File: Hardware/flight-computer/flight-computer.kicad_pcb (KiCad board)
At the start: 4 copper layers, 25.4 x 51.5 mm, 42 parts, among them J1 Conn_01x06_Pin, J2 Conn_01x06_Pin, J3 Power Connector, J4 Micro_SD_Card, J5 USB_C_Receptacle_USB2.0_16P, J6 Conn_01x02_Pin, Q1 DMN3404L, Q2 DMN3404L, U1 LMR51420X, U2 ESP32-S3-WROOM-1, U3 LSM6DSO32TR, U4 INA2180A1IDGKR

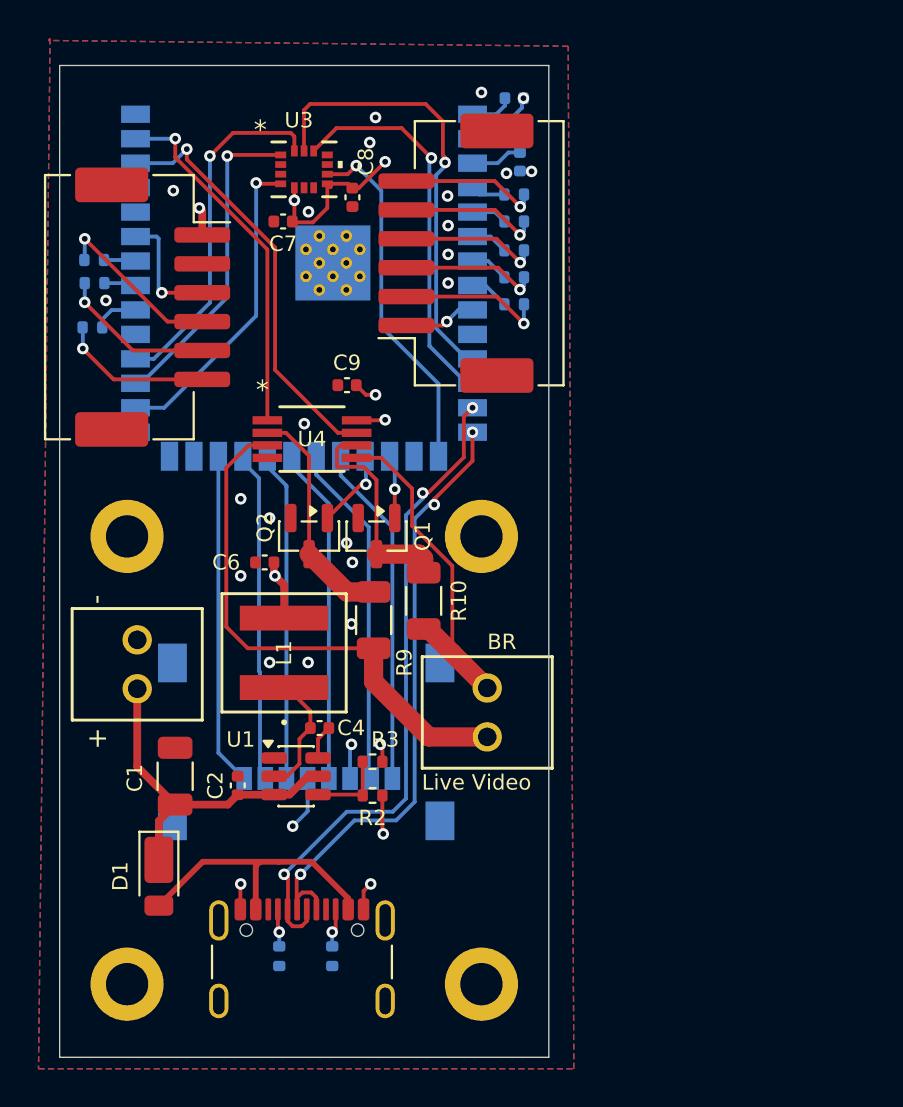
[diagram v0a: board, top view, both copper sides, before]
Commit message: added barometer and 10p conn to esp
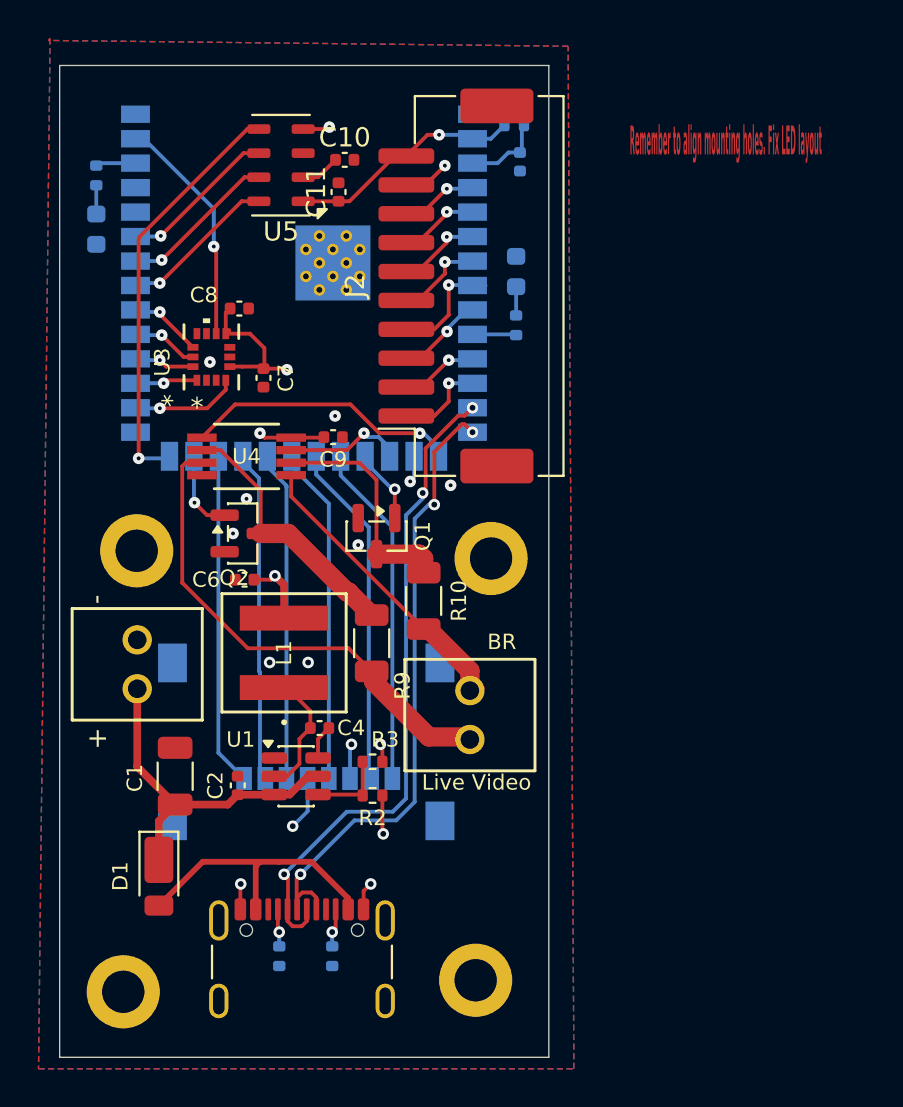
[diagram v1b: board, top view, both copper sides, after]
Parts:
- removed J1: Conn_01x06_Pin, Connector_JST:JST_ZE_SM06B-ZESS-TB_1x06-1MP_P1.50mm_Horizontal
- removed R11, R12, R13, R14, R15, R8: 200 Ohm, Resistor_SMD:R_0402_1005Metric
- added C10: 100nF, Capacitor_SMD:C_0402_1005Metric, F.Cu at (146.9, 83.6)
- added C11: 10uF, Capacitor_SMD:C_0402_1005Metric, F.Cu at (146.6, 85.3)
- added D2: LED, LED_SMD:LED_0603_1608Metric, B.Cu at (134.0, 87.2)
- added D3: LED, LED_SMD:LED_0603_1608Metric, B.Cu at (155.8, 89.4)
- added U5: MPL3115A2, Package_LGA:NXP_LGA-8_3x5mm_P1.25mm_H1.1mm, F.Cu at (143.6, 83.9)
- J2: value Conn_01x06_Pin -> Conn_01x10_Pin; footprint Connector_JST:JST_ZE_SM06B-ZESS-TB_1x06-1MP_P1.50mm_Horizontal -> Connector_JST:JST_ZE_SM10B-ZESS-TB_1x10-1MP_P1.50mm_Horizontal
- R10, R9: value 100 mOhm -> 15 mOhm
- R6, R7: value 200 Ohm -> 220
- moved H2 23.0 mm to (153.7, 126.2)
- moved H3 22.5 mm to (136.1, 103.9)
- moved R7 22.2 mm to (155.8, 92.2), turned to 90 degrees
- moved H1 18.9 mm to (154.5, 104.3)
- moved H4 18.6 mm to (135.4, 126.8)
- moved U3 10.9 mm to (140.0, 93.9), turned to 90 degrees
- moved C8 8.24 mm to (141.4, 91.4), turned to 0 degrees
- moved C7 8.19 mm to (142.7, 95.0), turned to -90 degrees
- moved R6 7.89 mm to (134.0, 84.5), turned to -90 degrees
- moved U4 3.52 mm to (141.8, 99.0)
- moved Q2 3.45 mm to (141.6, 103.0), turned to 0 degrees
- moved C9 2.79 mm to (146.3, 98.0), turned to 180 degrees
- moved J2 1.70 mm to (152.7, 90.2)
- moved C6 1.38 mm to (141.7, 105.4)
- moved R9 1.20 mm to (148.3, 108.7)
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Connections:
- J2 pad 1: FIN_RST -> FIN4_RX
- J2 pad 2: Net-(J2-Pin_2) -> FIN4_TX
- J2 pad 3: Net-(J2-Pin_3) -> FIN3_RX
- J2 pad 4: Net-(J2-Pin_4) -> FIN3_TX
- J2 pad 5: Net-(J2-Pin_5) -> FIN2_RX
- J2 pad 6: Net-(J2-Pin_6) -> FIN2_TX
- Q1 pad 1: Remote Start 1 -> Remote Start 2
- Q2 pad 1: Remote Start 2 -> Remote Start 1
- R6 pad 1: Net-(J1-Pin_6) -> Net-(U2-IO2)
- R6 pad 2: FIN_SCK -> Net-(D2-A)
- R7 pad 1: Net-(J1-Pin_4) -> Net-(U2-IO17)
- R7 pad 2: FIN_MOSI -> Net-(D3-A)
- U2 pad 10: unconnected-(U2-IO17-Pad10) -> Net-(U2-IO17)
- U2 pad 11: LSM_SCK -> FIN4_TX
- U2 pad 12: LSM_CS -> FIN4_RX
- U2 pad 15: LSM_INT2 -> IMP_OUT1
- U2 pad 17: Remote Start 1 -> IMP_OUT2
- U2 pad 25: unconnected-(U2-IO48-Pad25) -> Remote Start 1
- U2 pad 26: unconnected-(U2-IO45-Pad26) -> MPL_INT2
- U2 pad 31: unconnected-(U2-IO38-Pad31) -> LSM_SCK
- U2 pad 32: FIN_SCK -> LSM_CS
- U2 pad 33: FIN_MISO -> MPL_SCL
- U2 pad 34: FIN_MOSI -> MPL_SDA
- U2 pad 35: FIN_DRDY -> MPL_INT1
- U2 pad 38: IMP_OUT2 -> Net-(U2-IO2)
- U2 pad 39: IMP_OUT1 -> LSM_INT2
- U2 pad 4: FIN_CS1 -> FIN1_TX
- U2 pad 5: FIN_CS2 -> FIN1_RX
- U2 pad 6: FIN_CS3 -> FIN2_TX
- U2 pad 7: FIN_CS4 -> FIN2_RX
- U2 pad 8: FIN_CLK -> FIN3_TX
- U2 pad 9: FIN_RST -> FIN3_RX
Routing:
- net MPL_INT2: track 0.00 -> 21.7 mm, vias 0 -> 1
- net LSM_SCK: track 23.4 -> 3.47 mm
- net LSM_CS: track 20.1 -> 3.86 mm
- net IMP_OUT2: track 21.9 -> 6.26 mm
- net LSM_MOSI: track 18.6 -> 3.15 mm
- net LSM_MISO: track 16.8 -> 3.25 mm
- net LSM_INT1: track 16.8 -> 5.59 mm
- net +3.3V: track 25.0 -> 35.4 mm, vias 9 -> 7
- net Net-(J1-Pin_4): track 8.99 -> 0.00 mm, vias 1 -> 0
- net MPL_INT1: track 0.00 -> 8.27 mm, vias 0 -> 1
- net MPL_SCL: track 0.00 -> 8.22 mm, vias 0 -> 1
- net MPL_SDA: track 0.00 -> 8.21 mm, vias 0 -> 1
- net Net-(J1-Pin_5): track 8.14 -> 0.00 mm, vias 1 -> 0
- net Net-(J1-Pin_6): track 7.97 -> 0.00 mm, vias 1 -> 0
- net Net-(J2-Pin_2): track 7.68 -> 0.00 mm, vias 1 -> 0
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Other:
- board text added: "Remember to align mounting holes. Fix LED layout"
- board text removed: "fix me"

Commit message: aligned mounting holes
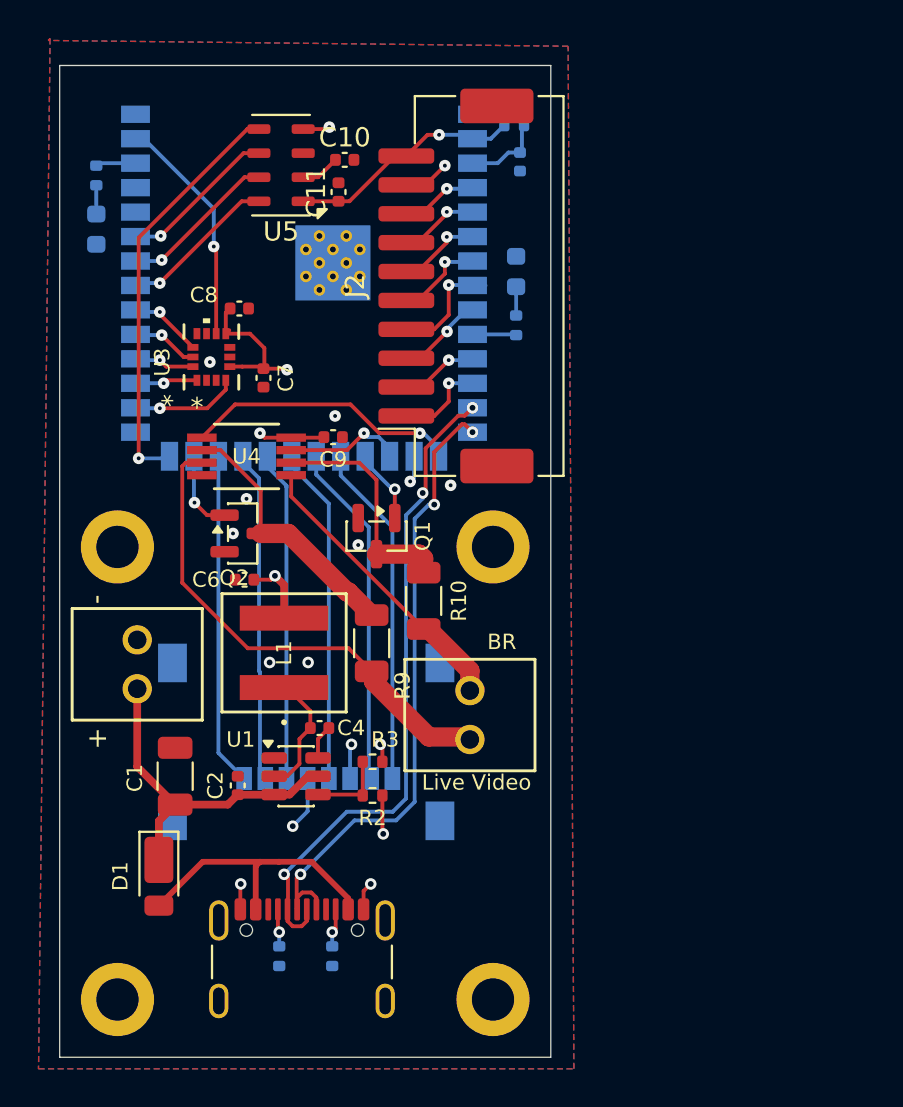
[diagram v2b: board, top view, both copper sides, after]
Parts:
- moved H2 1.35 mm to (154.6, 127.2)
- moved H3 1.02 mm to (135.1, 103.7)
- moved H1 0.61 mm to (154.6, 103.7)
- moved H4 0.50 mm to (135.1, 127.2)
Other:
- board size 25.4 x 51.5 mm -> 25.5 x 51.5 mm
- board text removed: "Remember to align mounting holes. Fix LED layout"
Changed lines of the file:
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@@
 		(allow_soldermask_bridges_in_footprints no)
 		(tenting front back)
-		(grid_origin 157.481895 78.746555)
+		(grid_origin 157.581895 130.246555)
 		(pcbplotparams
 			(layerselection 0x00000000_00000000_55555555_5755f5ff)
@@
 	(footprint "MountingHole:MountingHole_2.2mm_M2_DIN965_Pad"
 		(layer "F.Cu")
-		(at 153.681895 126.246555)
+		(at 154.581895 127.246555)
 		(descr "Mounting Hole 2.2mm, M2, generated by kicad-footprint-generator mountinghole.py")
 		(tags "mountinghole M2 DIN965")
@@
 	(footprint "MountingHole:MountingHole_2.2mm_M2_DIN965_Pad"
 		(layer "F.Cu")
-		(at 135.381895 126.846555)
+		(at 135.081895 127.246555)
 		(descr "Mounting Hole 2.2mm, M2, generated by kicad-footprint-generator mountinghole.py")
 		(tags "mountinghole M2 DIN965")
@@
 	(footprint "MountingHole:MountingHole_2.2mm_M2_DIN965_Pad"
 		(layer "F.Cu")
-		(at 154.481895 104.346555)
+		(at 154.581895 103.746555)
 		(descr "Mounting Hole 2.2mm, M2, generated by kicad-footprint-generator mountinghole.py")
 		(tags "mountinghole M2 DIN965")
@@
 	(footprint "MountingHole:MountingHole_2.2mm_M2_DIN965_Pad"
 		(layer "F.Cu")
-		(at 136.081895 103.946555)
+		(at 135.08 103.746555)
 		(descr "Mounting Hole 2.2mm, M2, generated by kicad-footprint-generator mountinghole.py")
 		(tags "mountinghole M2 DIN965")
@@
 	(gr_rect
 		(start 132.08 78.746555)
-		(end 157.48 130.246555)
+		(end 157.581895 130.246555)
 		(stroke
 			(width 0.05)
@@
 		(layer "Edge.Cuts")
 	)
-	(gr_text "Remember to align mounting holes. Fix LED layout"
-		(at 161.681895 83.546555 0)
-		(layer "F.Cu")
-		(effects
-			(font
-				(size 1.5 0.254)
-				(thickness 0.0635)
-				(bold yes)
-			)
-			(justify left bottom)
-		)
-	)
 	(gr_text "+"

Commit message: finalish board
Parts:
- D2, D3, R6, R7: moved to F.Cu
- moved D3 22.1 mm to (134.1, 93.5), turned to 90 degrees
- moved R7 22.1 mm to (134.1, 96.3)
- moved D2 0.96 mm to (134.0, 88.2)
- moved R6 0.96 mm to (134.0, 85.4)
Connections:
- D3 pad 1: GND -> Net-(D3-K)
- D3 pad 2: Net-(D3-A) -> +3.3V
- R7 pad 1: Net-(U2-IO17) -> Net-(U2-IO0)
- R7 pad 2: Net-(D3-A) -> Net-(D3-K)
- U2 pad 10: Net-(U2-IO17) -> unconnected-(U2-IO17-Pad10)
- U2 pad 27: unconnected-(U2-IO0-Pad27) -> Net-(U2-IO0)
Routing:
- net USB_D+: track 33.3 -> 37.5 mm
- net USB_D-: track 34.2 -> 37.9 mm
- net Net-(U2-IO0): track 0.00 -> 2.87 mm, vias 0 -> 1
- net Net-(U2-IO17): track 2.28 -> 0.00 mm
- net Net-(D3-A): track 1.49 -> 0.00 mm
- net Net-(D3-K): track 0.00 -> 1.49 mm
- net Net-(U2-IO2): track 2.09 -> 3.44 mm, vias 0 -> 1
- net +3.3V: track 35.4 -> 36.7 mm, vias 7 -> 8
- net Net-(J6-Pin_1): track 25.7 -> 25.2 mm
